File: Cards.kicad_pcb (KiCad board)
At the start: 2 copper layers, 63.5 x 88.9 mm, 8 parts

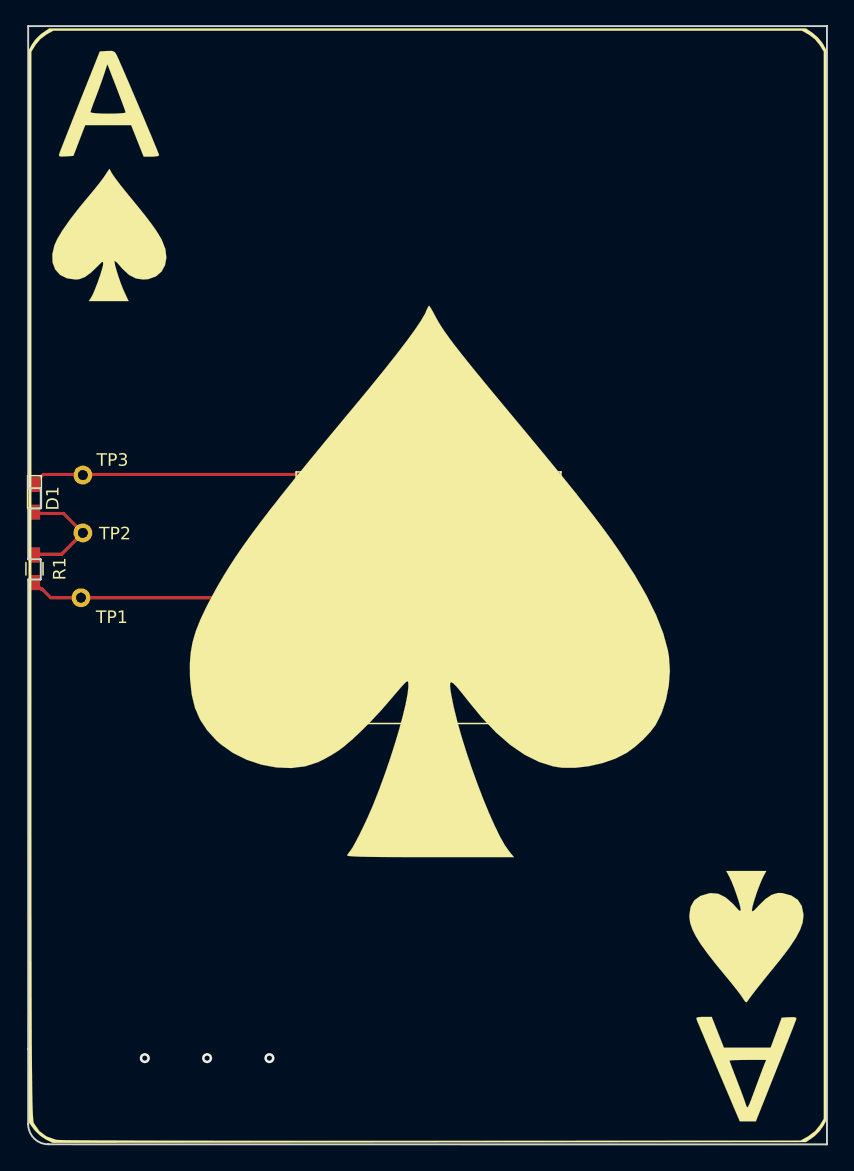
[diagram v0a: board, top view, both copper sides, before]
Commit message: Modified board edge to approx 1 in by 3 in and removed mask layers
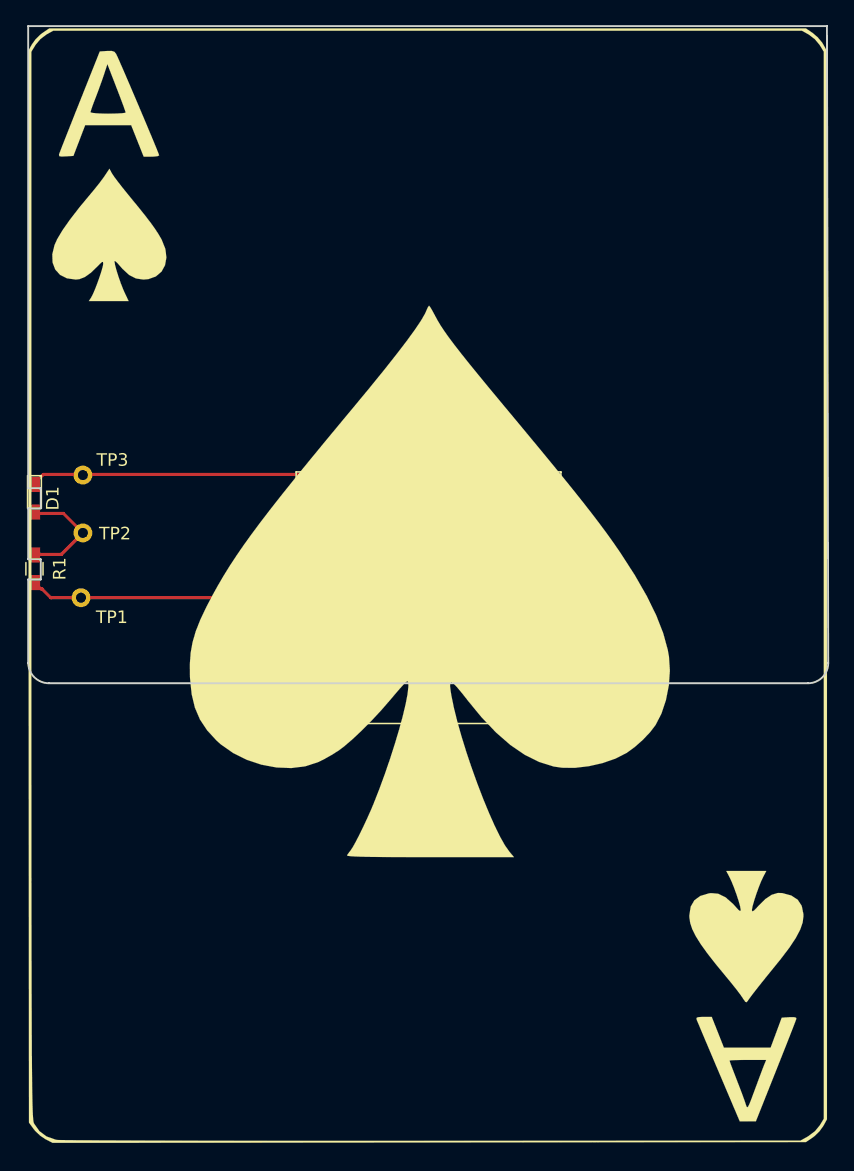
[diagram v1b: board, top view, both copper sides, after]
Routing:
- net (no net): vias 3 -> 0
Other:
- board size 63.5 x 88.9 mm -> 63.6 x 52.2 mm

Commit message: Modified board to just cover the test points and board edge
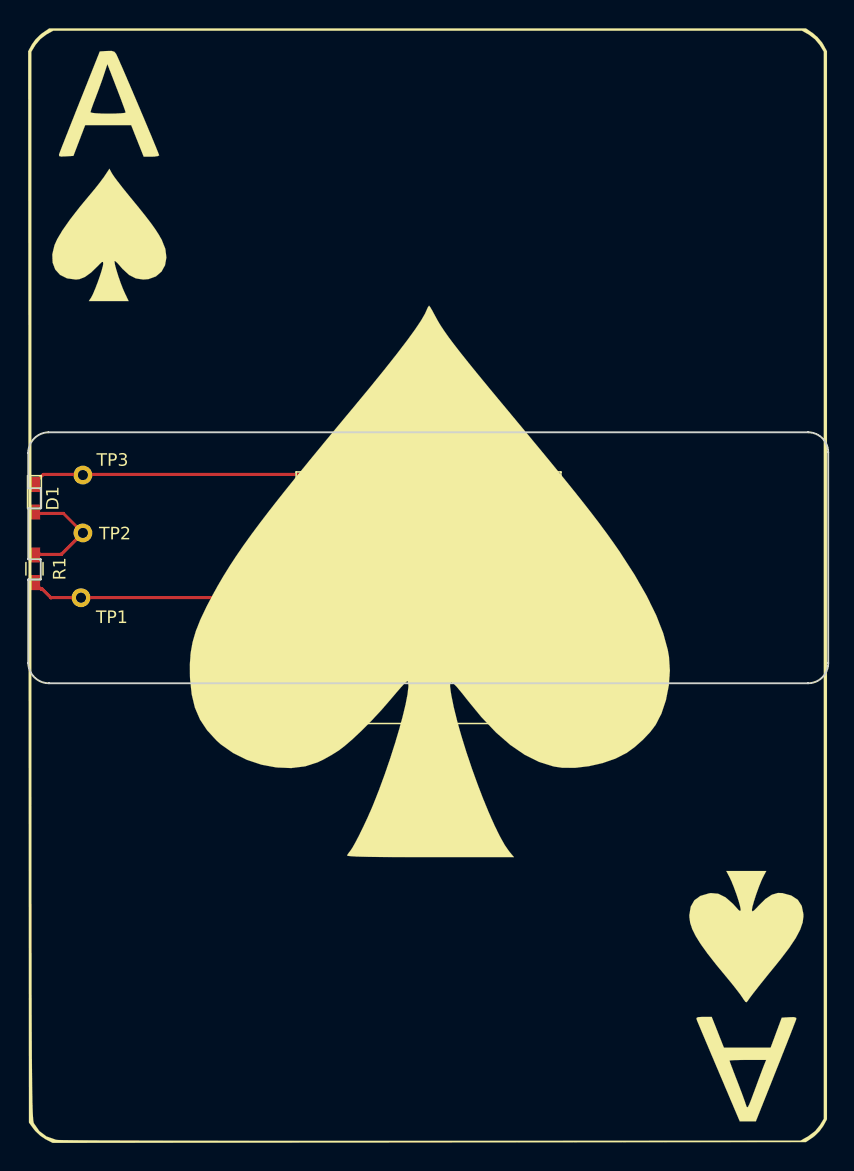
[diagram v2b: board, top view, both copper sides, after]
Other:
- board size 63.6 x 52.2 mm -> 63.6 x 20 mm
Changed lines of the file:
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@@
     (36 B.SilkS user)
     (37 F.SilkS user)
-    (38 B.Mask user hide)
-    (39 F.Mask user hide)
+    (38 B.Mask user)
+    (39 F.Mask user)
     (40 Dwgs.User user)
     (41 Cmts.User user)
@@
       (net 1 "Net-(BT1-Pad1)"))
   )
+  (gr_arc (start 150.9 94.85) (end 152.5 94.85) (angle -90) (layer Edge.Cuts) (width 0.15))
+  (gr_arc (start 90.550757 94.9) (end 90.500757 93.25) (angle -88.26429541) (layer Edge.Cuts) (width 0.15))
   (gr_arc (start 150.9 111.600757) (end 150.9 113.200757) (angle -90) (layer Edge.Cuts) (width 0.15))
   (gr_line (start 150.9 113.200757) (end 90.55 113.200757) (layer Edge.Cuts) (width 0.15))
@@
   (gr_line (start 88.9 103.35) (end 89.9 103.35) (layer Edge.Cuts) (width 0.15))
   (gr_line (start 89.9 104.95) (end 89.9 103.35) (layer Edge.Cuts) (width 0.15))
-  (gr_line (start 88.9 60.96) (end 88.9 97.7) (layer Edge.Cuts) (width 0.15))
+  (gr_line (start 88.9 94.9) (end 88.9 97.7) (layer Edge.Cuts) (width 0.15))
   (gr_line (start 89.9 97.7) (end 88.9 97.7) (layer Edge.Cuts) (width 0.15))
   (gr_line (start 89.9 99.3) (end 89.9 97.7) (layer Edge.Cuts) (width 0.15))
   (gr_line (start 88.9 99.3) (end 89.9 99.3) (layer Edge.Cuts) (width 0.15))
-  (gr_poly (pts (xy 88.9 149.86) (xy 152.4 149.86) (xy 152.4 60.96) (xy 88.9 60.96)) (layer F.Mask) (width 0.15))
-  (gr_poly (pts (xy 88.9 149.86) (xy 152.4 149.86) (xy 152.4 60.96) (xy 88.9 60.96)) (layer B.Mask) (width 0.15))
-  (gr_line (start 152.4 60.96) (end 152.5 111.600757) (layer Edge.Cuts) (width 0.15))
-  (gr_line (start 88.9 60.96) (end 152.4 60.96) (layer Edge.Cuts) (width 0.15))
+  (gr_line (start 152.5 94.85) (end 152.5 111.600757) (layer Edge.Cuts) (width 0.15))
+  (gr_line (start 90.500757 93.25) (end 150.9 93.25) (layer Edge.Cuts) (width 0.15))
   (segment (start 129.9 110) (end 133.5 106.4) (width 0.25) (layer F.Cu) (net 1))
   (segment (start 107.9 106.4) (end 111.5 110) (width 0.25) (layer F.Cu) (net 1))
